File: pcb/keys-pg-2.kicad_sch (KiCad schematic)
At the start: 28 parts

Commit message: pcb: added C and rmd unneeded hardware
Signed-off-by: Dylan Turner <dylan.turner@tutanota.com>
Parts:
- added S_REAL6: ~, COM-13834:COM13834, symbol COM-13834:COM-13834
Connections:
- net GND: now also S_REAL6.1
- new net KEY_REAL_6: S_REAL6.2
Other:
- note added: "Forgot the letter C So make a new 6 and put C where 6 was"
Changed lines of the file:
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@@
 		(company "Polymath-Studio")
 	)
+	(polyline
+		(pts
+			(xy 95.885 171.45) (xy 95.885 197.485)
+		)
+		(stroke
+			(width 0)
+			(type default)
+		)
+	)
 	(wire
 		(pts
@@
 		)
 	)
-	(polyline
-		(pts
-			(xy 38.1 171.45) (xy 63.5 171.45)
-		)
-		(stroke
-			(width 0)
-			(type default)
-		)
-	)
 	(wire
 		(pts
@@
 		)
 	)
+	(wire
+		(pts
+			(xy 43.18 189.23) (xy 45.72 189.23)
+		)
+		(stroke
+			(width 0)
+			(type default)
+		)
+	)
+	(polyline
+		(pts
+			(xy 24.13 171.45) (xy 24.13 197.485)
+		)
+		(stroke
+			(width 0)
+			(type default)
+		)
+	)
 	(polyline
 		(pts
@@
 		)
 	)
+	(wire
+		(pts
+			(xy 66.04 189.23) (xy 68.58 189.23)
+		)
+		(stroke
+			(width 0)
+			(type default)
+		)
+	)
 	(polyline
 		(pts
@@
 		)
 	)
+	(text "Forgot the letter C\nSo make a new 6\nand put C where 6 was"
+		(exclude_from_sim no)
+		(at 76.454 180.086 0)
+		(effects
+			(font
+				(size 1.27 1.27)
+			)
+		)
+	)
 	(text "Thumb Rows"
 		(exclude_from_sim no)
@@
 		)
 	)
+	(hierarchical_label "KEY_REAL_6"
+		(shape input)
+		(at 43.18 189.23 180)
+		(fields_autoplaced yes)
+		(effects
+			(font
+				(size 1.27 1.27)
+			)
+			(justify right)
+		)
+	)
 	(hierarchical_label "KEY_8"
 		(shape input)
@@
 	(symbol
 		(lib_id "COM-13834:COM-13834")
+		(at 45.72 189.23 0)
+		(unit 1)
+		(exclude_from_sim no)
+		(in_bom yes)
+		(on_board yes)
+		(dnp no)
+		(fields_autoplaced yes)
+		(property "Reference" "S_REAL6"
+			(at 55.88 182.88 0)
+			(effects
+				(font
+					(size 1.27 1.27)
+				)
+			)
+		)
+		(property "Value" "~"
+			(at 55.88 185.42 0)
+			(effects
+				(font
+					(size 1.27 1.27)
+				)
+			)
+		)
+		(property "Footprint" "COM-13834:COM13834"
+			(at 62.23 284.15 0)
+			(effects
+				(font
+					(size 1.27 1.27)
+				)
+				(justify left top)
+				(hide yes)
+			)
+		)
+		(property "Datasheet" "https://cdn.sparkfun.com/datasheets/Components/Switches/MX%20Series.pdf"
+			(at 62.23 384.15 0)
+			(effects
+				(font
+					(size 1.27 1.27)
+				)
+				(justify left top)
+				(hide yes)
+			)
+		)
+		(property "Description" "Pushbutton Switch SPST-NO Keyswitch Through Hole, Standard force, click tactile, PCB mount- MX1A-E1NW"
+			(at 45.72 189.23 0)
+			(effects
+				(font
+					(size 1.27 1.27)
+				)
+				(hide yes)
+			)
+		)
+		(property "Height" "15.2"
+			(at 62.23 584.15 0)
+			(effects
+				(font
+					(size 1.27 1.27)
+				)
+				(justify left top)
+				(hide yes)
+			)
+		)
+		(property "Mouser Part Number" "474-COM-13834"
+			(at 62.23 684.15 0)
+			(effects
+				(font
+					(size 1.27 1.27)
+				)
+				(justify left top)
+				(hide yes)
+			)
+		)
+		(property "Mouser Price/Stock" "https://www.mouser.co.uk/ProductDetail/SparkFun/COM-13834?qs=WyAARYrbSnYlamGcWwdgnQ%3D%3D"
+			(at 62.23 784.15 0)
+			(effects
+				(font
+					(size 1.27 1.27)
+				)
+				(justify left top)
+				(hide yes)
+			)
+		)
+		(property "Manufacturer_Name" "SparkFun"
+			(at 62.23 884.15 0)
+			(effects
+				(font
+					(size 1.27 1.27)
+				)
+				(justify left top)
+				(hide yes)
+			)
+		)
+		(property "Manufacturer_Part_Number" "COM-13834"
+			(at 62.23 984.15 0)
+			(effects
+				(font
+					(size 1.27 1.27)
+				)
+				(justify left top)
+				(hide yes)
+			)
+		)
+		(pin "2"
+		)
+		(pin "1"
+		)
+		(instances
+			(project "ps-ohk"
+				(path "/9764b4ba-7c88-49a9-89e6-e6f35382ac72/e06a5160-bd5e-4880-9a19-fab52aabf7b2"
+					(reference "S_REAL6")
+					(unit 1)
+				)
+			)
+		)
+	)
+	(symbol
+		(lib_id "COM-13834:COM-13834")
 		(at 152.4 142.24 270)
 		(unit 1)
@@
 					(unit 1)
 				)
+			)
+		)
+	)
+	(symbol
+		(lib_id "power:Earth")
+		(at 68.58 189.23 90)
+		(unit 1)
+		(exclude_from_sim no)
+		(in_bom yes)
+		(on_board yes)
+		(dnp no)
+		(fields_autoplaced yes)
+		(property "Reference" "#PWR012"
+			(at 74.93 189.23 0)
+			(effects
+				(font
+					(size 1.27 1.27)
+				)
+				(hide yes)
+			)
+		)
+		(property "Value" "GND"
+			(at 73.66 189.23 0)
+			(effects
+				(font
+					(size 1.27 1.27)
+				)
+			)
+		)
+		(property "Footprint" ""
+			(at 68.58 189.23 0)
+			(effects
+				(font
+					(size 1.27 1.27)
+				)
+				(hide yes)
+			)
+		)
+		(property "Datasheet" "~"
+			(at 68.58 189.23 0)
+			(effects
+				(font
+					(size 1.27 1.27)
+				)
+				(hide yes)
+			)
+		)
+		(property "Description" "Power symbol creates a global label with name \"Earth\""
+			(at 68.58 189.23 0)
+			(effects
+				(font
+					(size 1.27 1.27)
+				)
+				(hide yes)
+			)
+		)
+		(pin "1"
+		)
+		(instances
+			(project "ps-ohk"
+				(path "/9764b4ba-7c88-49a9-89e6-e6f35382ac72/e06a5160-bd5e-4880-9a19-fab52aabf7b2"
+					(reference "#PWR012")
+					(unit 1)
+				)

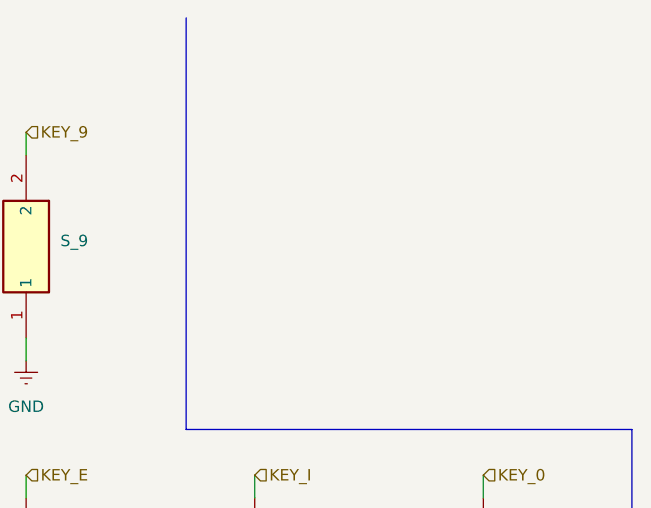
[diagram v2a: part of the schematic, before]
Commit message: pcb: add backspace and move k
Signed-off-by: Dylan Turner <dylan.turner@tutanota.com>
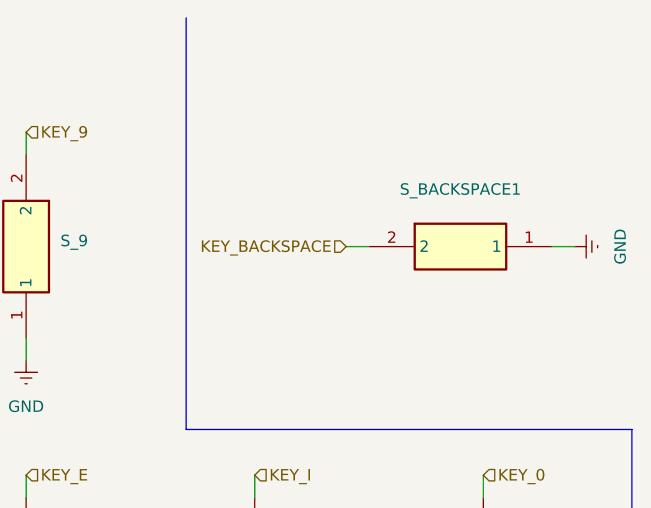
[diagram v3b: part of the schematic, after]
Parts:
- added S_BACKSPACE1: ~, COM-13834:COM13834, symbol COM-13834:COM-13834
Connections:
- net GND: now also S_BACKSPACE1.1
- new net KEY_BACKSPACE: S_BACKSPACE1.2
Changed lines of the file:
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@@
 	(wire
 		(pts
+			(xy 210.82 38.1) (xy 213.36 38.1)
+		)
+		(stroke
+			(width 0)
+			(type default)
+		)
+	)
+	(wire
+		(pts
 			(xy 177.8 124.46) (xy 177.8 127)
 		)
@@
 	(wire
 		(pts
+			(xy 187.96 38.1) (xy 190.5 38.1)
+		)
+		(stroke
+			(width 0)
+			(type default)
+		)
+	)
+	(wire
+		(pts
 			(xy 76.2 48.26) (xy 76.2 50.8)
 		)
@@
 		)
 	)
+	(hierarchical_label "KEY_BACKSPACE"
+		(shape input)
+		(at 187.96 38.1 180)
+		(fields_autoplaced yes)
+		(effects
+			(font
+				(size 1.27 1.27)
+			)
+			(justify right)
+		)
+	)
 	(hierarchical_label "KEY_5"
 		(shape input)
@@
 	)
 	(symbol
+		(lib_id "power:Earth")
+		(at 213.36 38.1 90)
+		(unit 1)
+		(exclude_from_sim no)
+		(in_bom yes)
+		(on_board yes)
+		(dnp no)
+		(fields_autoplaced yes)
+		(property "Reference" "#PWR029"
+			(at 219.71 38.1 0)
+			(effects
+				(font
+					(size 1.27 1.27)
+				)
+				(hide yes)
+			)
+		)
+		(property "Value" "GND"
+			(at 218.44 38.1 0)
+			(effects
+				(font
+					(size 1.27 1.27)
+				)
+			)
+		)
+		(property "Footprint" ""
+			(at 213.36 38.1 0)
+			(effects
+				(font
+					(size 1.27 1.27)
+				)
+				(hide yes)
+			)
+		)
+		(property "Datasheet" "~"
+			(at 213.36 38.1 0)
+			(effects
+				(font
+					(size 1.27 1.27)
+				)
+				(hide yes)
+			)
+		)
+		(property "Description" "Power symbol creates a global label with name \"Earth\""
+			(at 213.36 38.1 0)
+			(effects
+				(font
+					(size 1.27 1.27)
+				)
+				(hide yes)
+			)
+		)
+		(pin "1"
+		)
+		(instances
+			(project "ps-ohk"
+				(path "/9764b4ba-7c88-49a9-89e6-e6f35382ac72/e06a5160-bd5e-4880-9a19-fab52aabf7b2"
+					(reference "#PWR029")
+					(unit 1)
+				)
+			)
+		)
+	)
+	(symbol
 		(lib_id "COM-13834:COM-13834")
 		(at 76.2 27.94 270)
@@
 					(unit 1)
 				)
+			)
+		)
+	)
+	(symbol
+		(lib_id "COM-13834:COM-13834")
+		(at 190.5 38.1 0)
+		(unit 1)
+		(exclude_from_sim no)
+		(in_bom yes)
+		(on_board yes)
+		(dnp no)
+		(fields_autoplaced yes)
+		(property "Reference" "S_BACKSPACE1"
+			(at 200.66 31.75 0)
+			(effects
+				(font
+					(size 1.27 1.27)
+				)
+			)
+		)
+		(property "Value" "~"
+			(at 200.66 34.29 0)
+			(effects
+				(font
+					(size 1.27 1.27)
+				)
+			)
+		)
+		(property "Footprint" "COM-13834:COM13834"
+			(at 207.01 133.02 0)
+			(effects
+				(font
+					(size 1.27 1.27)
+				)
+				(justify left top)
+				(hide yes)
+			)
+		)
+		(property "Datasheet" "https://cdn.sparkfun.com/datasheets/Components/Switches/MX%20Series.pdf"
+			(at 207.01 233.02 0)
+			(effects
+				(font
+					(size 1.27 1.27)
+				)
+				(justify left top)
+				(hide yes)
+			)
+		)
+		(property "Description" "Pushbutton Switch SPST-NO Keyswitch Through Hole, Standard force, click tactile, PCB mount- MX1A-E1NW"
+			(at 190.5 38.1 0)
+			(effects
+				(font
+					(size 1.27 1.27)
+				)
+				(hide yes)
+			)
+		)
+		(property "Height" "15.2"
+			(at 207.01 433.02 0)
+			(effects
+				(font
+					(size 1.27 1.27)
+				)
+				(justify left top)
+				(hide yes)
+			)
+		)
+		(property "Mouser Part Number" "474-COM-13834"
+			(at 207.01 533.02 0)
+			(effects
+				(font
+					(size 1.27 1.27)
+				)
+				(justify left top)
+				(hide yes)
+			)
+		)
+		(property "Mouser Price/Stock" "https://www.mouser.co.uk/ProductDetail/SparkFun/COM-13834?qs=WyAARYrbSnYlamGcWwdgnQ%3D%3D"
+			(at 207.01 633.02 0)
+			(effects
+				(font
+					(size 1.27 1.27)
+				)
+				(justify left top)
+				(hide yes)
+			)
+		)
+		(property "Manufacturer_Name" "SparkFun"
+			(at 207.01 733.02 0)
+			(effects
+				(font
+					(size 1.27 1.27)
+				)
+				(justify left top)
+				(hide yes)
+			)
+		)
+		(property "Manufacturer_Part_Number" "COM-13834"
+			(at 207.01 833.02 0)
+			(effects
+				(font
+					(size 1.27 1.27)
+				)
+				(justify left top)
+				(hide yes)
+			)
+		)
+		(pin "2"
+		)
+		(pin "1"
+		)
+		(instances
+			(project "ps-ohk"
+				(path "/9764b4ba-7c88-49a9-89e6-e6f35382ac72/e06a5160-bd5e-4880-9a19-fab52aabf7b2"
+					(reference "S_BACKSPACE1")
+					(unit 1)
+				)
